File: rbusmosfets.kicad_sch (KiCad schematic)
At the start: 19 parts, among them J1 RBUS, J4 Conn_01x02_Male, Q4 PXP012-30QLJ, Q5 PXP012-30QLJ, Q6 PXP012-30QLJ, Q7 PXP012-30QLJ, U10 LTC4412xS6, U9 LTC4412xS6

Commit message: PCB layout work
pcb layout work
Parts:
- renumbered TP5 to TP3
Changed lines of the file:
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@@
   (symbol (lib_id "Connector:TestPoint") (at 50.8 172.72 270) (unit 1)
     (in_bom yes) (on_board yes) (dnp no)
-    (property "Reference" "TP5" (at 49.53 175.26 90)
+    (property "Reference" "TP3" (at 49.53 175.26 90)
       (effects (font (size 1.27 1.27)) (justify left))
     )

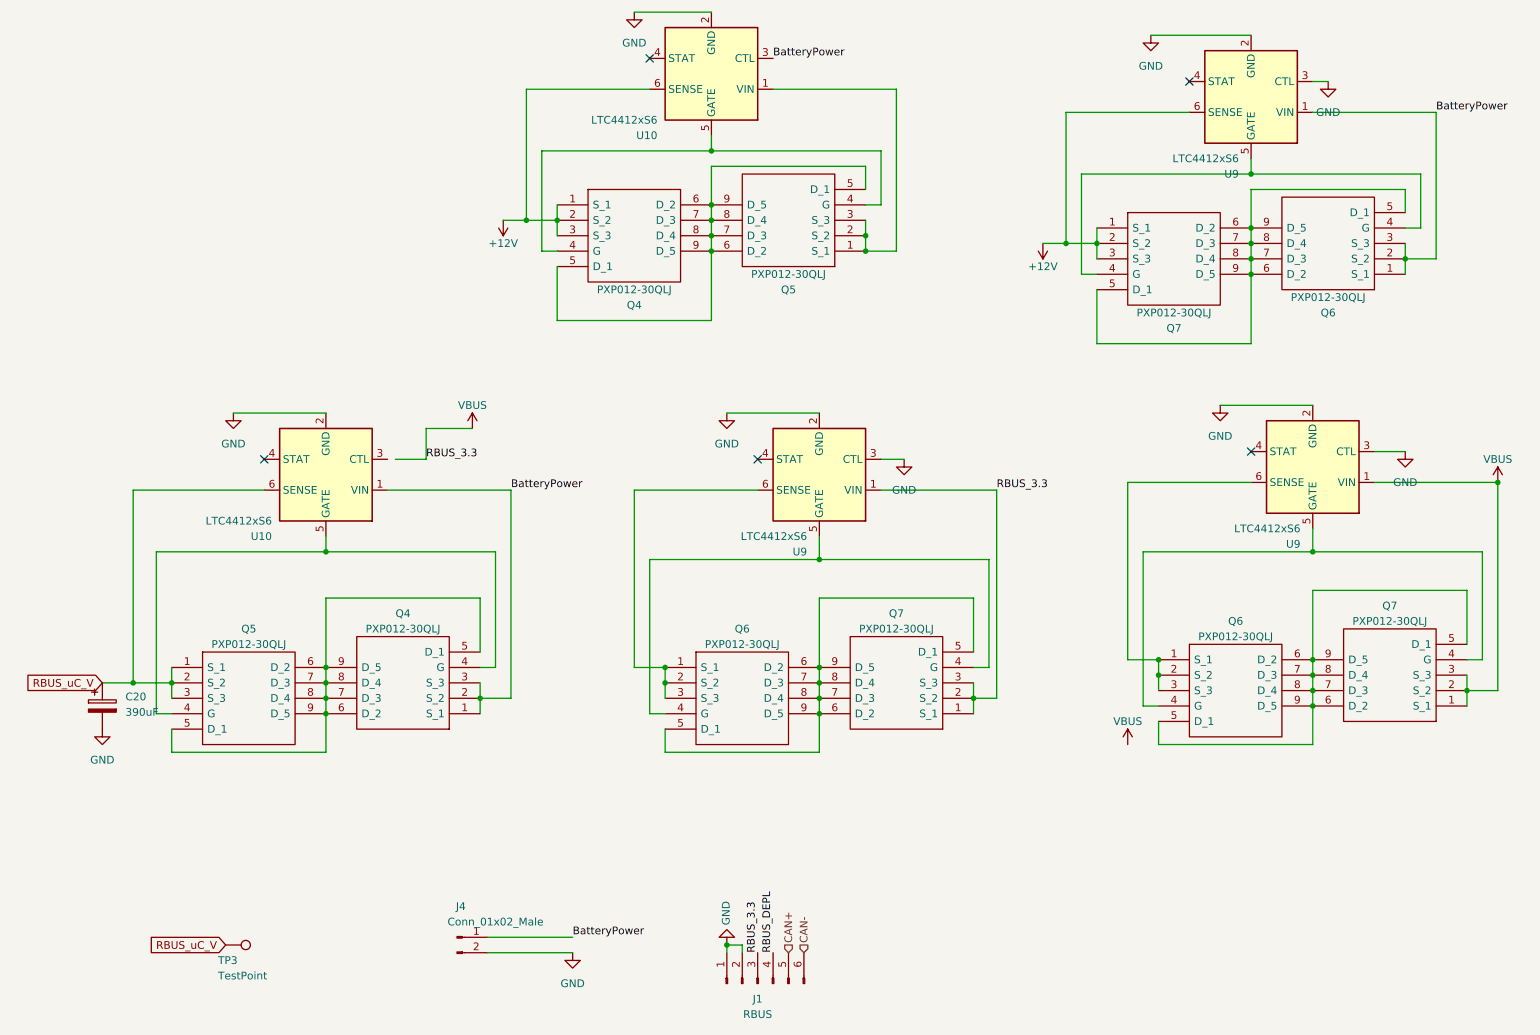
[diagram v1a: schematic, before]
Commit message: schematic review updated
fixed:
-pin 1 on the bootjumper is missing a connection. 
- Move the SD card to a 2nd SPI bus (so a 2nd set of MISO, MOSI, SCLK) as the rest of the bus is blocked while data is written to it, which would interrupt sensor readings. 
- Add a pull-up resistor on the DET_A pin of the micro SD card, and also connect that pin to the esp32 (picture from pickle) 
- VDD on the IMU (U7) is not connected to any power, should be connected to 3.3V 
- Turns out CAN capacitors C18, C19 actually aren’t needed. It’s up to you if you want to keep them, but if you do keep them could you change their value to “DNP” (stands for Do not place) 
-  Add test points to lines which can potentially cause issues. Most of the time this just means places that are connected to the ESP32, but especially places like the SPI lines (including chip selects). Also, add test points to TXD and RXD on the esp32 in case we have to solder to them for programming  

Servo Buck Converter 
- Pin 29 missing ground connection 
-  Add a text label with the part number of the 2.1uH inductor 

LTC4412s 
- No power net connected to Vin 
- stocky diodes replaced logic mosfets
- switched mosfets around so S is common
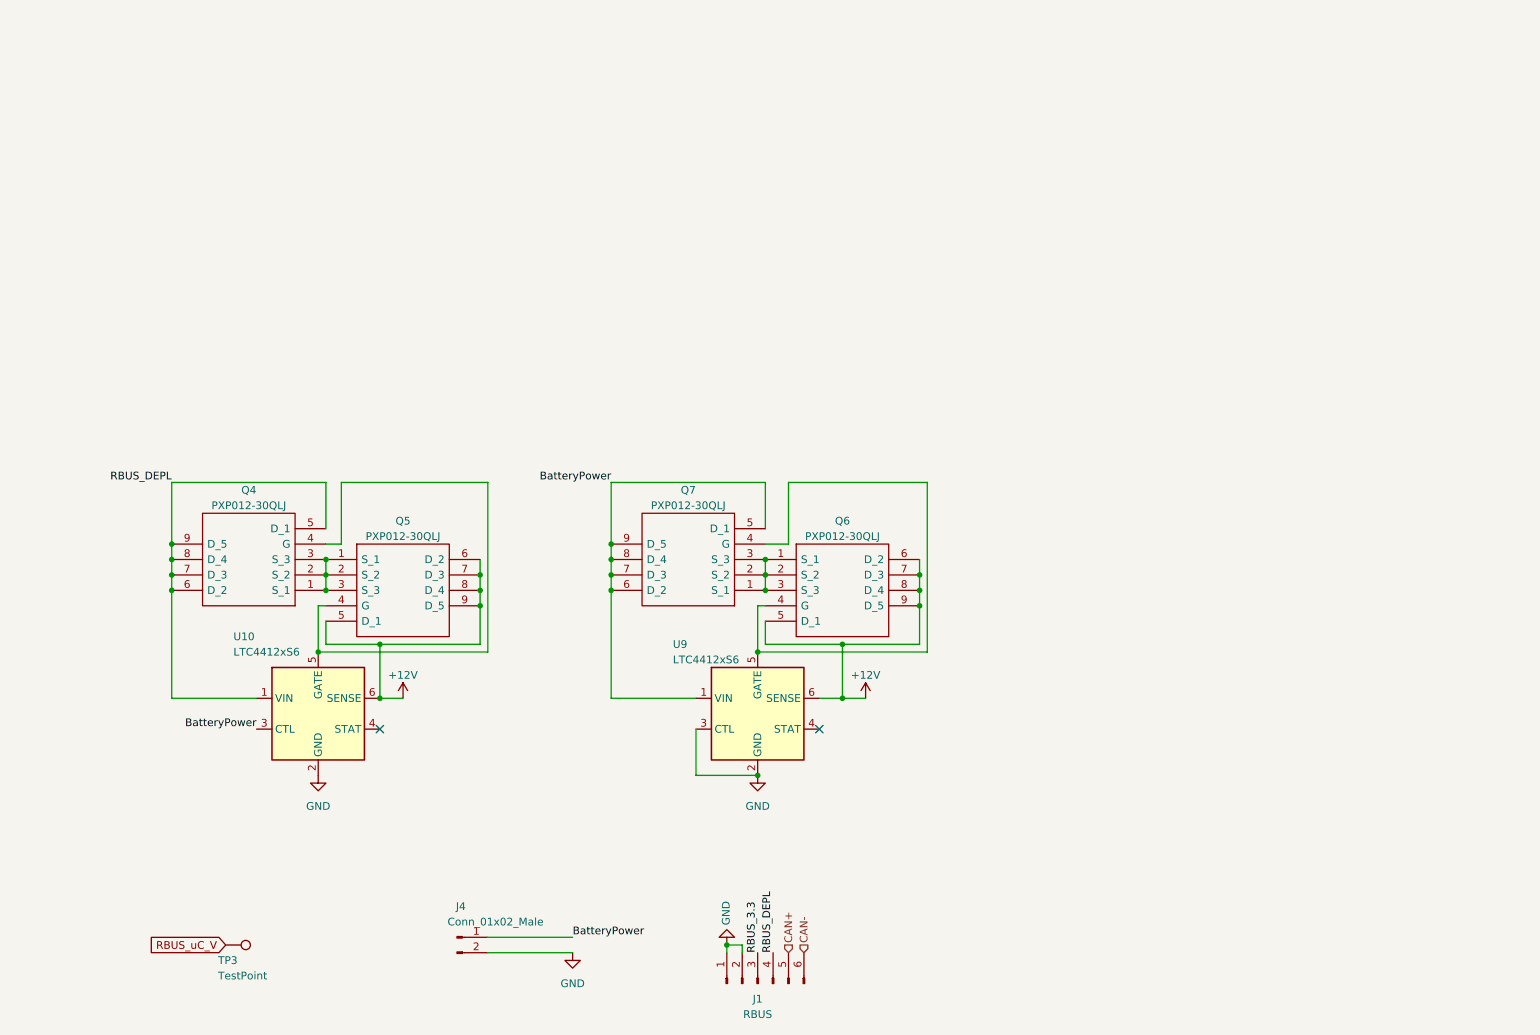
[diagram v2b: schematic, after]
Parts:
- removed C20: 390uF, Capacitor_SMD:CP_Elec_8x11.9, symbol Device:C_Polarized
- removed Q4, Q5, Q6 (x2), Q7 (x2): PXP012-30QLJ, iclr:PXP01230QLJ, symbol iclr:PXP012-30QLJ
- removed U10, U9 (x2): LTC4412xS6, Package_TO_SOT_SMD:TSOT-23-6, symbol Power_Management:LTC4412xS6
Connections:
- net +12V: now also Q5.5 (D_1), Q5.6 (D_2), Q5.7 (D_3), Q5.8 (D_4), Q5.9 (D_5), Q6.5 (D_1), Q6.6 (D_2), Q6.7 (D_3), Q6.8 (D_4), Q6.9 (D_5); no longer Q4.1 (S_1), Q4.2 (S_2), Q4.3 (S_3), Q7.1 (S_1), Q7.2 (S_2), Q7.3 (S_3)
- net BatteryPower: now also Q7.5 (D_1), Q7.6 (D_2), Q7.7 (D_3), Q7.8 (D_4), Q7.9 (D_5); no longer Q6.1 (S_1), Q6.2 (S_2), Q6.3 (S_3)
- net RBUS_DEPL: now also Q4.5 (D_1), Q4.6 (D_2), Q4.7 (D_3), Q4.8 (D_4), Q4.9 (D_5), U10.1 (VIN)
- net at Q5.1 (S_1), Q5.2 (S_2), Q5.3 (S_3): now also Q4.1 (S_1), Q4.2 (S_2), Q4.3 (S_3); no longer U10.1 (VIN)
- net VBUS renamed RBUS_3.3
- new net: Q6.1 (S_1), Q6.2 (S_2), Q6.3 (S_3), Q7.1 (S_1), Q7.2 (S_2), Q7.3 (S_3)
- no-connect marks 5 -> 2
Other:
- moved on the sheet: Q4, Q5, Q6, Q7, U10, U9

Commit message: I don't want to lose all my changes so I will commit, commit.
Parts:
- added D3, D4, D5: D_Schottky, Diode_SMD:D_SOD-323, symbol Device:D_Schottky
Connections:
- net BatteryPower: now also D3.2 (A)
- net RBUS_3.3: now also D4.2 (A)
- net RBUS_uC_V: now also D3.1 (K), D4.1 (K), D5.1 (K)
- new net VBUS: D5.2 (A)
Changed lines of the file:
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@@
   (junction (at 165.1 114.3) (diameter 0) (color 0 0 0 0)
   )
+  (junction (at 63.5 46.99) (diameter 0) (color 0 0 0 0)
+  )
   (junction (at 114.3 109.22) (diameter 0) (color 0 0 0 0)
   )
@@
   )
   (junction (at 133.35 172.72) (diameter 0) (color 0 0 0 0)
+  )
+  (junction (at 63.5 53.34) (diameter 0) (color 0 0 0 0)
   )
   (junction (at 92.71 116.84) (diameter 0) (color 0 0 0 0)
@@
     (stroke (width 0) (type default))
   )
+  (wire (pts (xy 48.26 59.69) (xy 55.88 59.69))
+    (stroke (width 0) (type default))
+  )
   (wire (pts (xy 41.91 106.68) (xy 41.91 96.52))
     (stroke (width 0) (type default))
@@
     (stroke (width 0) (type default))
   )
+  (wire (pts (xy 63.5 53.34) (xy 63.5 59.69))
+    (stroke (width 0) (type default))
+  )
   (wire (pts (xy 139.7 123.19) (xy 152.4 123.19))
     (stroke (width 0) (type default))
@@
     (stroke (width 0) (type default))
   )
+  (wire (pts (xy 63.5 46.99) (xy 63.5 53.34))
+    (stroke (width 0) (type default))
+  )
   (wire (pts (xy 67.31 111.76) (xy 67.31 114.3))
     (stroke (width 0) (type default))
@@
     (stroke (width 0) (type default))
   )
+  (wire (pts (xy 48.26 53.34) (xy 55.88 53.34))
+    (stroke (width 0) (type default))
+  )
+  (wire (pts (xy 71.12 46.99) (xy 63.5 46.99))
+    (stroke (width 0) (type default))
+  )
   (wire (pts (xy 114.3 132.08) (xy 128.27 132.08))
     (stroke (width 0) (type default))
@@
   )
   (wire (pts (xy 92.71 116.84) (xy 92.71 114.3))
+    (stroke (width 0) (type default))
+  )
+  (wire (pts (xy 48.26 46.99) (xy 55.88 46.99))
     (stroke (width 0) (type default))
   )
@@
   (label "BatteryPower" (at 55.88 137.16 180) (fields_autoplaced)
     (effects (font (size 1.27 1.27)) (justify right bottom))
+  )
+  (label "RBUS_3.3" (at 48.26 53.34 180) (fields_autoplaced)
+    (effects (font (size 1.27 1.27)) (justify right bottom))
+  )
+  (label "BatteryPower" (at 48.26 46.99 180) (fields_autoplaced)
+    (effects (font (size 1.27 1.27)) (justify right bottom))
+  )
+  (global_label "RBUS_uC_V" (shape input) (at 71.12 46.99 0) (fields_autoplaced)
+    (effects (font (size 1.27 1.27)) (justify left))
+    (property "Intersheetrefs" "${INTERSHEET_REFS}" (at 83.8944 46.99 0)
+      (effects (font (size 1.27 1.27)) (justify left) hide)
+    )
   )
   (global_label "RBUS_uC_V" (shape input) (at 50.8 172.72 180) (fields_autoplaced)
@@
     )
   )
+  (symbol (lib_id "power:VBUS") (at 48.26 59.69 0) (unit 1)
+    (in_bom yes) (on_board yes) (dnp no) (fields_autoplaced)
+    (property "Reference" "#PWR045" (at 48.26 63.5 0)
+      (effects (font (size 1.27 1.27)) hide)
+    )
+    (property "Value" "VBUS" (at 48.26 55.88 0)
+      (effects (font (size 1.27 1.27)))
+    )
+    (property "Footprint" "" (at 48.26 59.69 0)
+      (effects (font (size 1.27 1.27)) hide)
+    )
+    (property "Datasheet" "" (at 48.26 59.69 0)
+      (effects (font (size 1.27 1.27)) hide)
+    )
+    (pin "1")
+    (instances
+      (project "Canardboard"
+        (path "/7db990e4-92e1-4f99-b4d2-435bbec1ba83/972bc3cd-df5c-4105-af8a-a8e2a9c5e16b"
+          (reference "#PWR045") (unit 1)
+        )
+      )
+    )
+  )
   (symbol (lib_id "power:GND") (at 133.35 172.72 180) (unit 1)
     (in_bom yes) (on_board yes) (dnp no)
@@
     )
   )
+  (symbol (lib_id "Device:D_Schottky") (at 59.69 46.99 180) (unit 1)
+    (in_bom yes) (on_board yes) (dnp no) (fields_autoplaced)
+    (property "Reference" "D3" (at 60.0075 41.91 0)
+      (effects (font (size 1.27 1.27)))
+    )
+    (property "Value" "D_Schottky" (at 60.0075 44.45 0)
+      (effects (font (size 1.27 1.27)))
+    )
+    (property "Footprint" "Diode_SMD:D_SOD-323" (at 59.69 46.99 0)
+      (effects (font (size 1.27 1.27)) hide)
+    )
+    (property "Datasheet" "~" (at 59.69 46.99 0)
+      (effects (font (size 1.27 1.27)) hide)
+    )
+    (pin "1")
+    (pin "2")
+    (instances
+      (project "Canardboard"
+        (path "/7db990e4-92e1-4f99-b4d2-435bbec1ba83/972bc3cd-df5c-4105-af8a-a8e2a9c5e16b"
+          (reference "D3") (unit 1)
+        )
+      )
+    )
+  )
   (symbol (lib_id "power:GND") (at 66.04 144.78 0) (unit 1)
     (in_bom yes) (on_board yes) (dnp no)
@@
         (path "/7db990e4-92e1-4f99-b4d2-435bbec1ba83/972bc3cd-df5c-4105-af8a-a8e2a9c5e16b"
           (reference "#PWR036") (unit 1)
+        )
+      )
+    )
+  )
+  (symbol (lib_id "Device:D_Schottky") (at 59.69 53.34 180) (unit 1)
+    (in_bom yes) (on_board yes) (dnp no) (fields_autoplaced)
+    (property "Reference" "D4" (at 60.0075 48.26 0)
+      (effects (font (size 1.27 1.27)))
+    )
+    (property "Value" "D_Schottky" (at 60.0075 50.8 0)
+      (effects (font (size 1.27 1.27)))
+    )
+    (property "Footprint" "Diode_SMD:D_SOD-323" (at 59.69 53.34 0)
+      (effects (font (size 1.27 1.27)) hide)
+    )
+    (property "Datasheet" "~" (at 59.69 53.34 0)
+      (effects (font (size 1.27 1.27)) hide)
+    )
+    (pin "1")
+    (pin "2")
+    (instances
+      (project "Canardboard"
+        (path "/7db990e4-92e1-4f99-b4d2-435bbec1ba83/972bc3cd-df5c-4105-af8a-a8e2a9c5e16b"
+          (reference "D4") (unit 1)
         )
       )
@@
         )
       )
+    )
+  )
+  (symbol (lib_id "Device:D_Schottky") (at 59.69 59.69 180) (unit 1)
+    (in_bom yes) (on_board yes) (dnp no) (fields_autoplaced)
+    (property "Reference" "D5" (at 60.0075 54.61 0)
+      (effects (font (size 1.27 1.27)))
+    )
+    (property "Value" "D_Schottky" (at 60.0075 57.15 0)
+      (effects (font (size 1.27 1.27)))
+    )
+    (property "Footprint" "Diode_SMD:D_SOD-323" (at 59.69 59.69 0)
+      (effects (font (size 1.27 1.27)) hide)
+    )
+    (property "Datasheet" "~" (at 59.69 59.69 0)
+      (effects (font (size 1.27 1.27)) hide)
+    )
+    (pin "1")
+    (pin "2")
+    (instances
+      (project "Canardboard"
+        (path "/7db990e4-92e1-4f99-b4d2-435bbec1ba83/972bc3cd-df5c-4105-af8a-a8e2a9c5e16b"
+          (reference "D5") (unit 1)
+        )
+      )

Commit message: weird 3v3 and 3.3v bug
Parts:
- added C20, C22: 1uF, Capacitor_SMD:C_0402_1005Metric, symbol Device:C_Small
- added JP3: SolderJumper_2_Open, Jumper:SolderJumper-2_P1.3mm_Open_RoundedPad1.0x1.5mm, symbol Jumper:SolderJumper_2_Open
- added R15, R42, R44, R46: 570, Resistor_SMD:R_0402_1005Metric, symbol Device:R_Small
- added R16, R23, R43, R45: 1.5k, Resistor_SMD:R_0402_1005Metric, symbol Device:R_Small
- added R47: 100k, Resistor_SMD:R_0402_1005Metric, symbol Device:R_Small
- added U5: 74AHC1G00, Package_TO_SOT_SMD:SOT-353_SC-70-5, symbol 74xGxx:74AHC1G00
- added U6: 74AHC1G08, Package_TO_SOT_SMD:SOT-353_SC-70-5, symbol 74xGxx:74AHC1G08
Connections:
- net BatteryPower: now also R16.1, R43.1; no longer U10.3 (CTL)
- net GND: now also C20.1, C22.1, JP3.2 (B), R15.2, R42.2, R44.2, R46.2, U5.3 (GND), U6.3 (GND); no longer U9.3 (CTL)
- net RBUS_DEPL: now also R23.2, R45.2
- new net: R43.2, R44.1, U6.1
- new net: R45.1, R46.1, U6.2
- new net: R47.2, U10.3 (CTL), U6.4
- new net: R15.1, R16.2, U5.1
- new net: R23.1, R42.1, U5.2
- new net: JP3.1 (A), U5.4, U9.3 (CTL)
- new net +3.3V: C20.2, C22.2, R47.1, U5.5 (VCC), U6.5 (VCC)
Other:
- moved on the sheet: Q4, Q5, Q6, Q7, U10, U9
